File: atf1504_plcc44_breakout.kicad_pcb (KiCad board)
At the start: 2 copper layers, 80.6 x 20.3 mm, 9 parts, among them J1 Atmel-JTAG-10, J2 Conn_01x17, J3 Conn_01x17, U1 ATF1504AS-xJx44

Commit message: Update
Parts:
- added C6: 100n, Capacitor_SMD:C_0805_2012Metric_Pad1.18x1.45mm_HandSolder, B.Cu at (165.9, 62.2)
- added X1: xMHz, Oscillator:Oscillator_SMD_IQD_IQXO70-4Pin_7.5x5.0mm_HandSoldering, F.Cu at (166.0, 62.2)
- C1: renamed from locked; footprint Capacitor_SMD:C_0805_2012Metric_Pad1.18x1.45mm_HandSolder -> Capacitor_THT:CP_Radial_D4.0mm_P1.50mm; moved to F.Cu
- J2, J3: value Conn_01x17 -> Conn_01x18
- moved C1 0.67 mm to (129.8, 62.4), turned to 0 degrees
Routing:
- net VCC: track 66.2 -> 111.4 mm, vias 2 -> 3
- net /I/GCLK1: track 17.3 -> 59.1 mm, vias 0 -> 2
- net GND: track 140.0 -> 144.1 mm, vias 2 -> 3
- net /B14: track 61.1 -> 62.6 mm
- net /B16: track 58.8 -> 59.9 mm
- net /D33: track 49.1 -> 49.8 mm

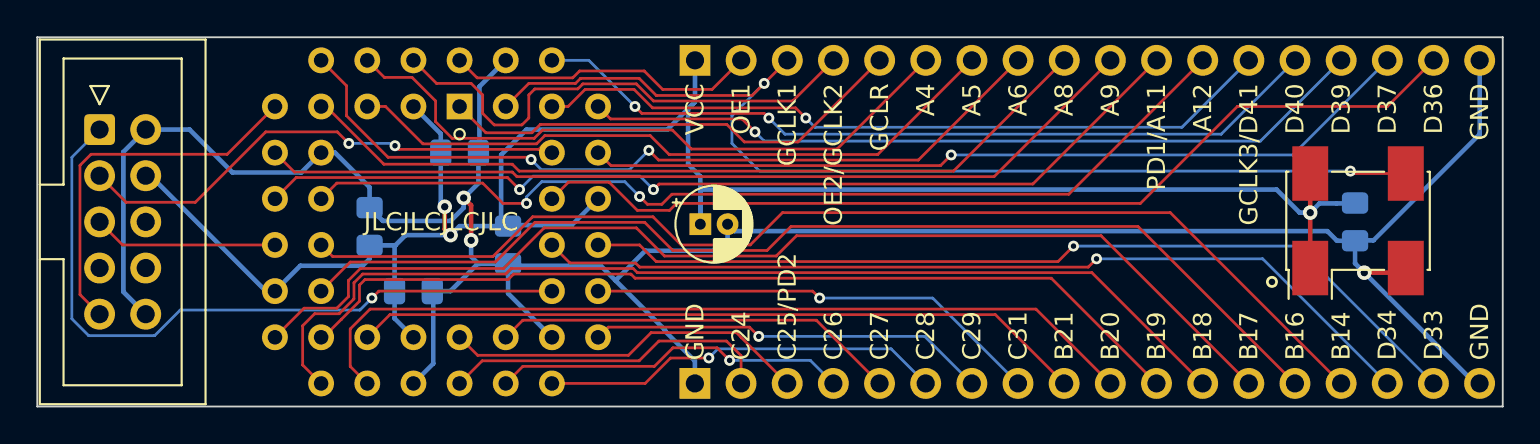
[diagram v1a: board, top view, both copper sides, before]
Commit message: Revert oscillator addition
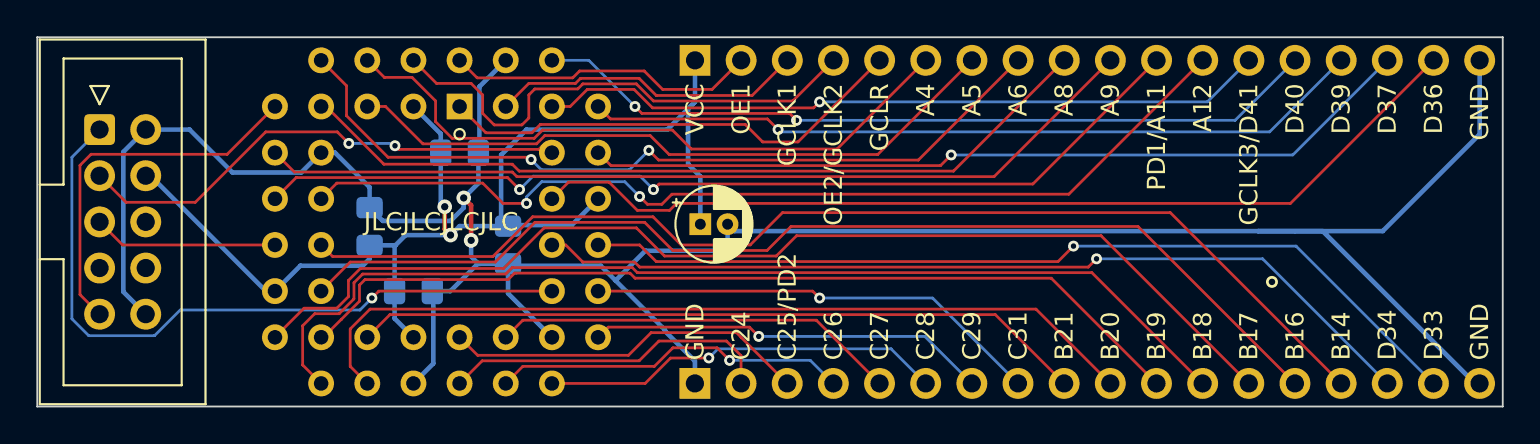
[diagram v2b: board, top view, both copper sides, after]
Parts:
- removed C6: 100n, Capacitor_SMD:C_0805_2012Metric_Pad1.18x1.45mm_HandSolder
- removed X1: xMHz, Oscillator:Oscillator_SMD_IQD_IQXO70-4Pin_7.5x5.0mm_HandSoldering
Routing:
- net VCC: track 111.4 -> 67.5 mm, vias 3 -> 2
- net /I/GCLK1: track 59.1 -> 17.3 mm, vias 2 -> 0
- net GND: track 144.1 -> 145.9 mm, vias 3 -> 2
- net /D41/GCLK3: track 41.1 -> 40.2 mm
- net /D40: track 44.3 -> 43.6 mm

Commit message: Add pin numbers for global inputs and re-order them
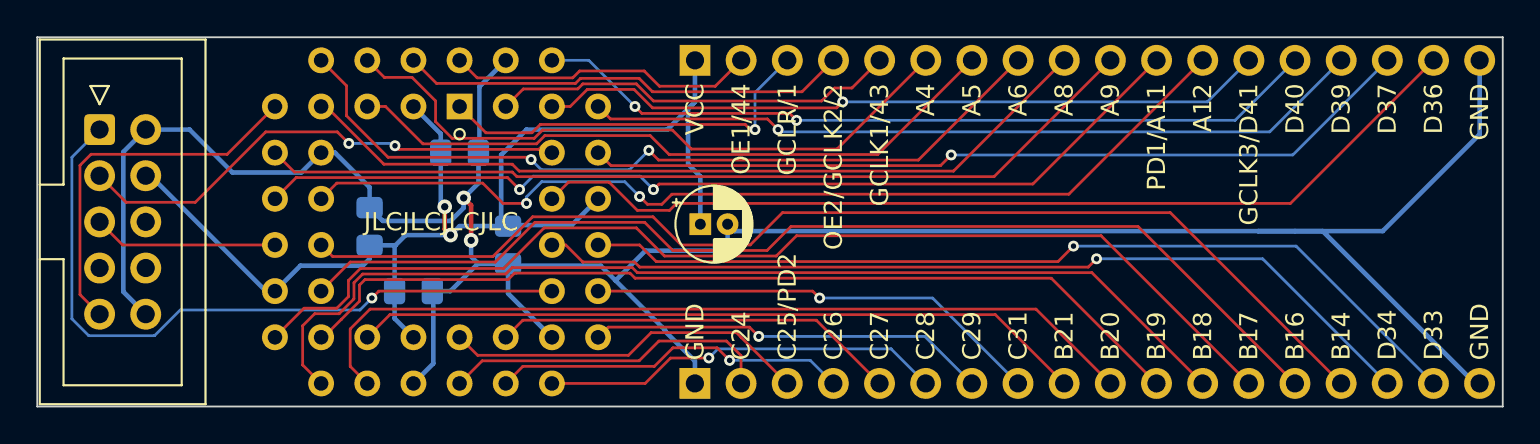
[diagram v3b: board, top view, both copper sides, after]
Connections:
- J3 pad 3: /I/GCLK1 -> /I/GCLR
- J3 pad 5: /I/GCLR -> /I/GCLK1
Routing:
- net /I/GCLK1: track 17.3 -> 22.4 mm
- net /I/GCLR: track 26.2 -> 21.7 mm, vias 0 -> 1
- net /I/OE2/GCLK2: track 28.2 -> 24.8 mm
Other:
- board text added: "ATF1504 / ATF1502 Breakout 2023-07-15 - Rev B Adrien Kohlbecker"
- board text added: "GCLK1/43"
- board text added: "GCLR/1"
- board text added: "OE1/44"
- board text added: "OE2/GCLK2/2"
- board text removed: "ATF1504 Breakout 2023-06-17 - Rev A Adrien Kohlbecker"
- board text removed: "GCLK1"
- board text removed: "GCLR"
- board text removed: "OE1"
- board text removed: "OE2/GCLK2"
